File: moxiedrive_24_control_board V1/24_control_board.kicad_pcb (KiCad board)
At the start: 2 copper layers, 80 x 50 mm, 127 parts, among them J1 Conn_01x03, J401 USB_C_Receptacle_USB2.0, J501 Unused_IO, J601 Conn_01x02, J602 Conn_01x02, J603 Conn_01x02, J901 Conn_02x10, K1 SERVO, K101 SERVO, P101 Conn_01x08, P102 Serial1/tim4, P103 I2C, P104 HALL/Encoder, P110 jst gh vert, P501 SWD_DEBUG, Q1001 60v 1a fet, Q1002 60v 1a fet, Q1003 60v 1a fet, Q601 60v 1a fet, Q602 60v 1a fet, SW501 SW_Push, U201 ME2188, U202 TPS561201, U301 WT51822-S4AT, U402 USBLC6-2, U501 STM32F40X_LQFP64, U701 TJA1051T-3, U801 BMI160, X501 16MHz 10ppm

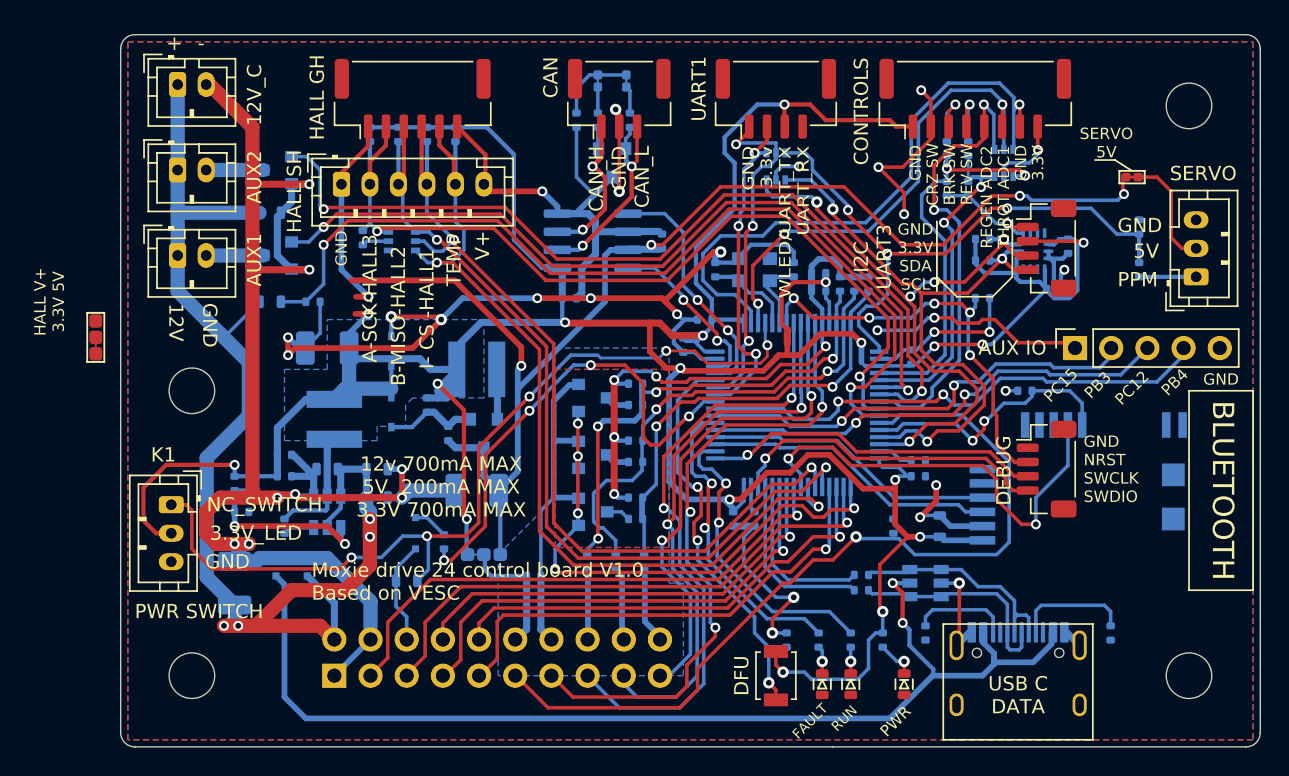
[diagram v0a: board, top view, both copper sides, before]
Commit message: fix misplaced component
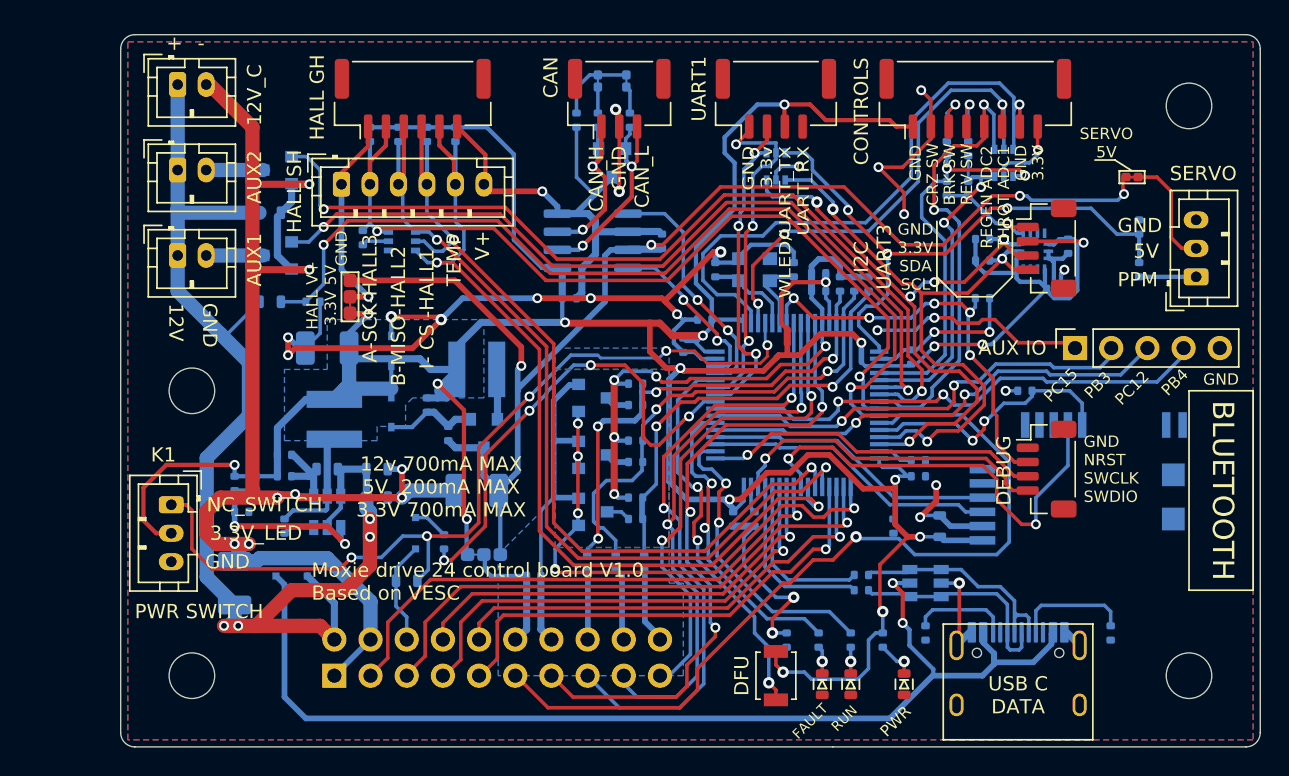
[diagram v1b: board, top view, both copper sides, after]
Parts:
- moved JP102 18.1 mm to (107.1, 88.4)
